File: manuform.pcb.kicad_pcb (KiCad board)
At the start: 2 copper layers, 100 x 90 mm, 48 parts, among them J1 Conn_01x04, J2 Conn_01x04, J3 Conn_01x04, SW1 SW_DIP_x01, SW2 SW_DIP_x01, SW3 SW_DIP_x01, SW4 SW_DIP_x01

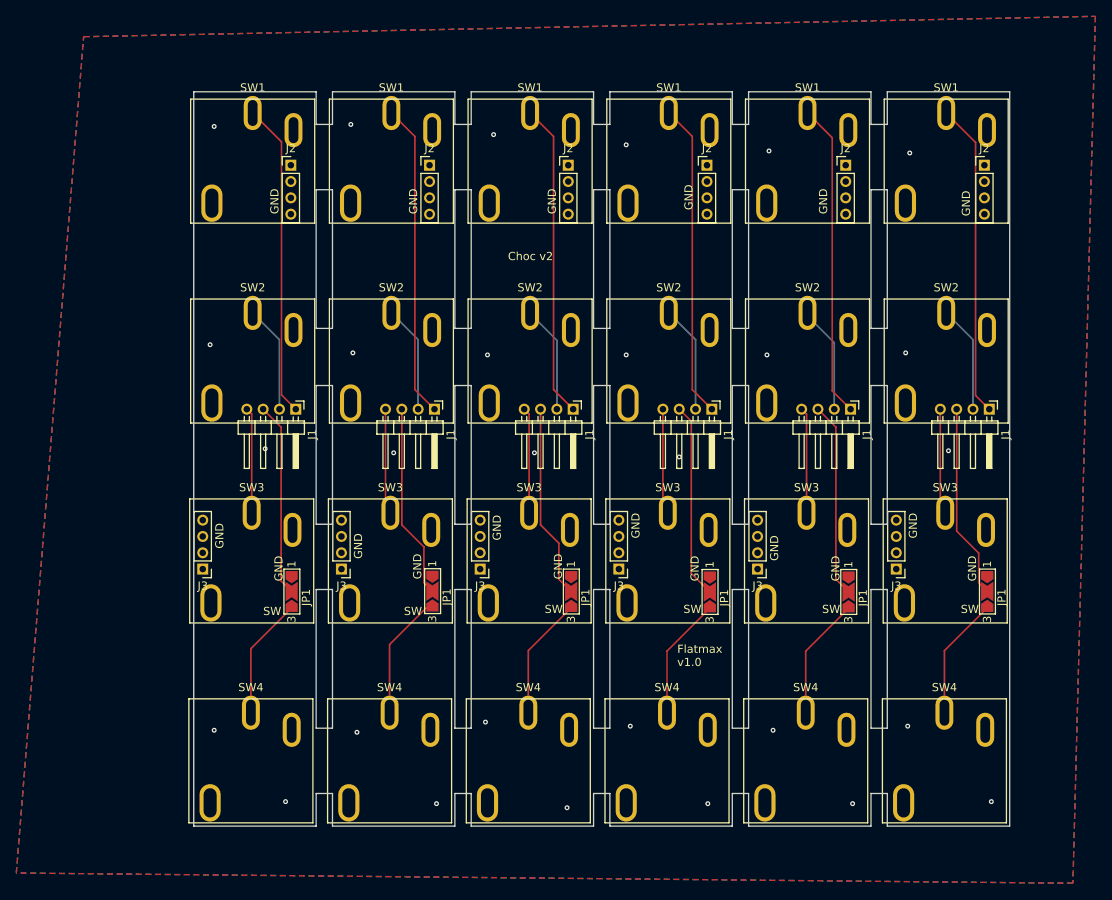
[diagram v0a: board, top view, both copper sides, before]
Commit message: fixed sizing for choc v2 with cosmos keys
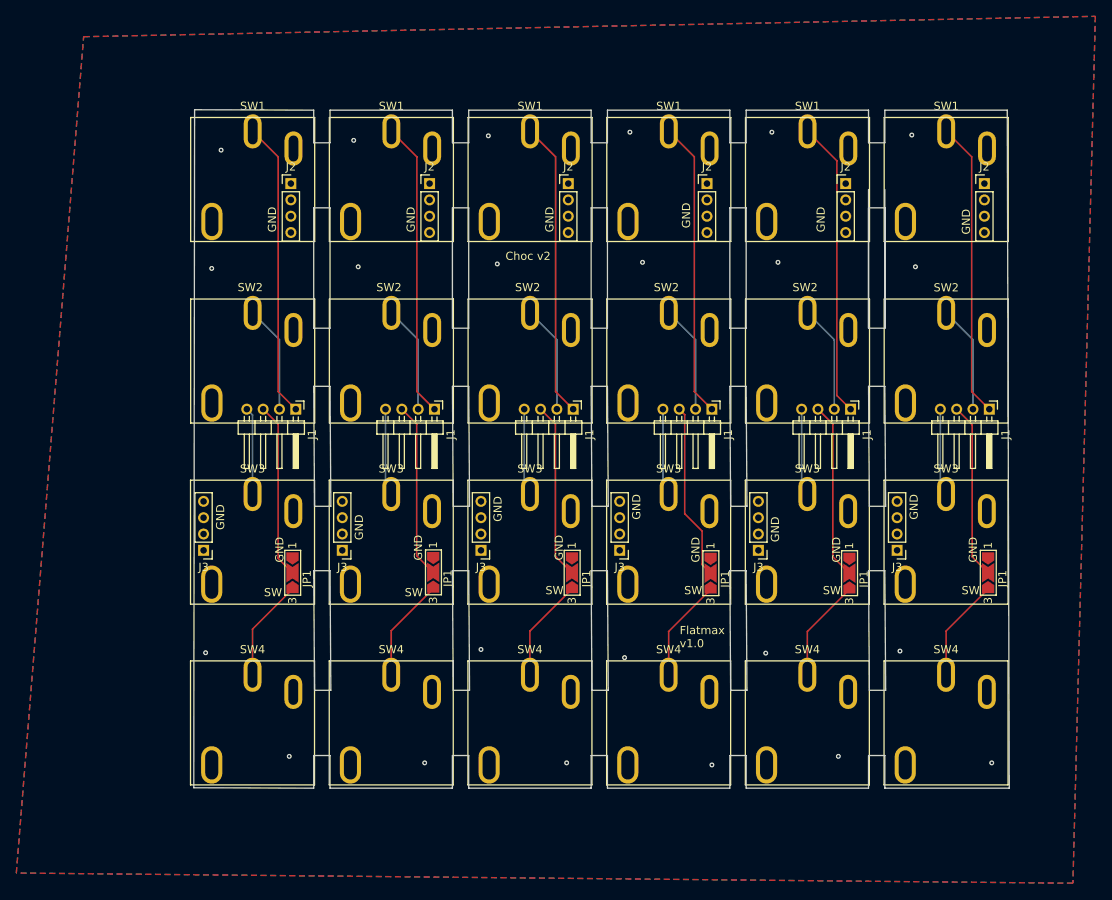
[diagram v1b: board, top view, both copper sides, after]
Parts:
- moved SW4 4.65 mm to (178.2, 114.3)
- moved SW4 4.65 mm to (161.2, 114.3)
- moved SW4 4.65 mm to (212.2, 114.3)
- moved SW4 4.65 mm to (246.2, 114.3)
- moved SW4 4.65 mm to (229.2, 114.3)
- moved SW4 4.65 mm to (195.2, 114.3)
- moved J3 2.30 mm to (240.2, 93.2)
- moved J3 2.30 mm to (155.2, 93.2)
- moved J3 2.30 mm to (223.2, 93.2)
- moved J3 2.30 mm to (206.2, 93.2)
- moved J3 2.30 mm to (172.2, 93.2)
- moved J3 2.30 mm to (189.2, 93.2)
- moved JP1 2.30 mm to (251.3, 96.0)
- moved JP1 2.30 mm to (217.3, 96.0)
- moved JP1 2.30 mm to (166.1, 96.0)
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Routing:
- net Net-(JP1-B): track 90.4 -> 75.6 mm
- net Net-(J1-Pin_4): track 77.7 -> 64.1 mm
- net Net-(J1-Pin_3): track 143.4 -> 129.8 mm
- net Net-(J1-Pin_1): track 230.9 -> 217.4 mm
- net GND: vias 29 -> 23
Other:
- board size 100 x 90 mm -> 99.9 x 83.1 mm
